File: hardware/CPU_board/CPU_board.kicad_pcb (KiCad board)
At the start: 4 copper layers, 51.2 x 25.8 mm, 111 parts, among them J1 TF TF-018 1.5mm, J2 SOUTH, J3 NORTH, J4 Conn_01x6_Male, J5 Conn_01x03, J6 JTAG, J8 Conn_01x10_Male, U1 EA3036A, U2 W25Q32JVZPIQ, U3 D1s-eLQFP128, U4 PAD30, U5 PAD30, U6 PAD30, U7 PAD30, U8 PAD30, U9 PAD30, X1 24MHz, X2 32.768KHz

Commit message: fixed mixup of pins G5/G4 (3rd diff pair ODD) and DE/PCLK (3rd diff pair EVEN), now with correct polarity for diff pairs
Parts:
- added R32: 10k, Resistor_SMD:R_0402_1005Metric, B.Cu at (101.6, 103.3)
- added R35: 10k, Resistor_SMD:R_0402_1005Metric, B.Cu at (101.6, 102.3)
- added R36: 10k, Resistor_SMD:R_0402_1005Metric, B.Cu at (105.2, 111.0)
- added R40: 10k, Resistor_SMD:R_0402_1005Metric, B.Cu at (106.2, 111.0)
- moved R30 3.79 mm to (107.0, 105.5)
- moved C37 3.05 mm to (105.0, 113.7), turned to -90 degrees
- moved C2 1.88 mm to (106.2, 113.9), turned to 90 degrees
- moved G*** 1.56 mm to (103.8, 102.9)
- moved R21 0.41 mm to (99.7, 105.2)
- moved C4 0.40 mm to (99.7, 106.1)
- moved C7 0.38 mm to (99.7, 104.2)
- moved C5 0.38 mm to (99.7, 103.3)
- moved C35 0.31 mm to (101.9, 109.9)
- moved C32 0.25 mm to (100.0, 109.9)
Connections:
- J2 pad 3: /LCD_V3P -> /LCD_V3N
- J2 pad 5: /LCD_V3N -> /LCD_V3P
- J3 pad 3: /LCD_U3P -> /LCD_U3N
- J3 pad 5: /LCD_U3N -> /LCD_U3P
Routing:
- net GND: track 210.5 -> 189.6 mm, vias 55 -> 54
- net 3V3: track 213.4 -> 226.3 mm
- net /PSEL: track 23.2 -> 13.5 mm
- net /SDA2: track 8.75 -> 12.4 mm
- net VSYS: track 24.0 -> 21.8 mm
- net /SCK: track 24.1 -> 22.4 mm
- net /SDA: track 24.8 -> 23.2 mm
- net /SCK2: track 8.59 -> 10.2 mm
- net /LCD_V3N: track 15.9 -> 14.4 mm
- net /LCD_D9: track 18.7 -> 17.8 mm
- net /X32KIN: track 6.42 -> 5.52 mm
- net /TP-Y2: track 24.7 -> 25.5 mm
- net /LCD_D8: track 19.7 -> 20.5 mm
- net /LCD_U3P: track 13.3 -> 14.1 mm
- net /LCD_V3P: track 14.0 -> 14.6 mm
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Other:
- board text added: "CPU board v0.11"
- board text added: "VERSION:"
- board text removed: "CPU board"
- board text removed: "Memory Card"

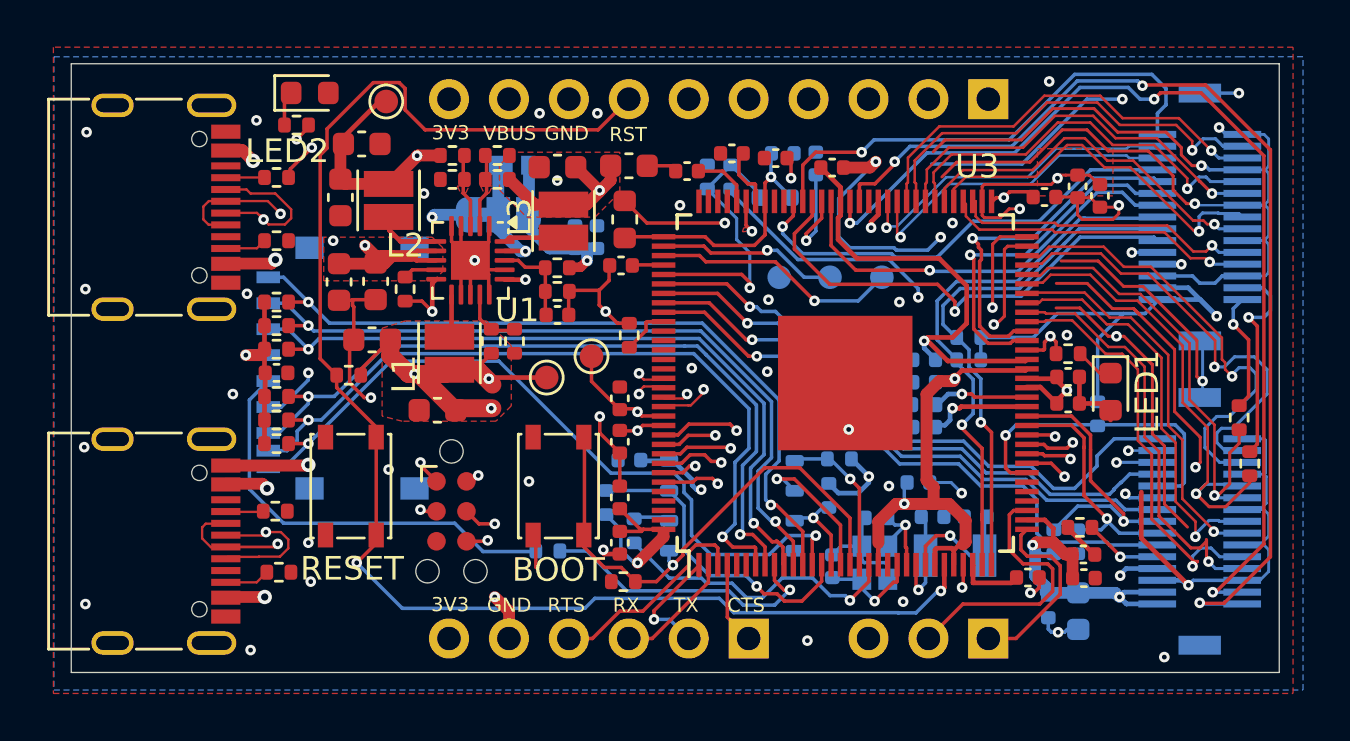
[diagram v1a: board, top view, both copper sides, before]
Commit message: review and update manufacturing constraints (via size, etc.)
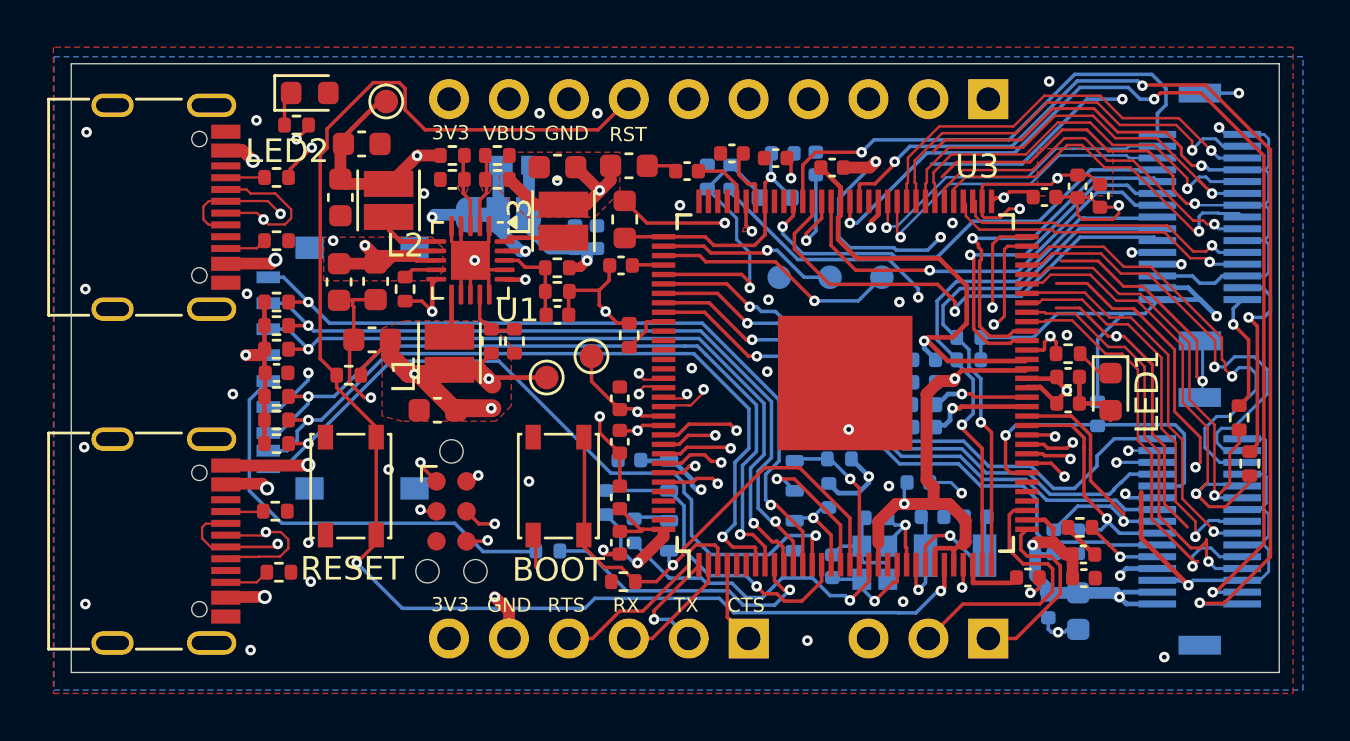
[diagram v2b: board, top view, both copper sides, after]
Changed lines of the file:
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@@
 	(via
 		(at 73.5928 107.702)
-		(size 0.6096)
-		(drill 0.3048)
+		(size 0.6)
+		(drill 0.35)
 		(layers "F.Cu" "B.Cu")
 		(net 14)
@@
 	)
 	(segment
+		(start 80.996048 111.377)
+		(end 83.2078 111.377)
+		(width 0.15)
+		(layer "B.Cu")
+		(net 21)
+	)
+	(segment
+		(start 72.4678 110.177)
+		(end 79.796048 110.177)
+		(width 0.15)
+		(layer "B.Cu")
+		(net 21)
+	)
+	(segment
+		(start 79.796048 110.177)
+		(end 80.996048 111.377)
+		(width 0.15)
+		(layer "B.Cu")
+		(net 21)
+	)
+	(segment
+		(start 71.0928 104.952)
+		(end 71.0928 108.802)
+		(width 0.15)
+		(layer "B.Cu")
+		(net 21)
+	)
+	(segment
+		(start 83.2078 111.377)
+		(end 83.2328 111.352)
+		(width 0.15)
+		(layer "B.Cu")
+		(net 21)
+	)
+	(segment
+		(start 71.0928 108.802)
+		(end 72.4678 110.177)
+		(width 0.15)
+		(layer "B.Cu")
+		(net 21)
+	)
+	(segment
 		(start 71.8928 104.152)
 		(end 71.0928 104.952)
-		(width 0.15)
-		(layer "B.Cu")
-		(net 21)
-	)
-	(segment
-		(start 83.2078 111.377)
-		(end 83.2328 111.352)
-		(width 0.15)
-		(layer "B.Cu")
-		(net 21)
-	)
-	(segment
-		(start 71.0928 108.727)
-		(end 72.5428 110.177)
-		(width 0.15)
-		(layer "B.Cu")
-		(net 21)
-	)
-	(segment
-		(start 72.5428 110.177)
-		(end 79.796048 110.177)
-		(width 0.15)
-		(layer "B.Cu")
-		(net 21)
-	)
-	(segment
-		(start 79.796048 110.177)
-		(end 80.996048 111.377)
-		(width 0.15)
-		(layer "B.Cu")
-		(net 21)
-	)
-	(segment
-		(start 80.996048 111.377)
-		(end 83.2078 111.377)
-		(width 0.15)
-		(layer "B.Cu")
-		(net 21)
-	)
-	(segment
-		(start 71.0928 104.952)
-		(end 71.0928 108.727)
 		(width 0.15)
 		(layer "B.Cu")
@@
 	(via
 		(at 71.8428 108.702)
-		(size 0.6096)
-		(drill 0.3048)
+		(size 0.6)
+		(drill 0.35)
 		(layers "F.Cu" "B.Cu")
 		(net 41)
@@
 	(via
 		(at 71.247828 94.817428)
-		(size 0.6096)
-		(drill 0.3048)
+		(size 0.6)
+		(drill 0.35)
 		(layers "F.Cu" "B.Cu")
 		(net 41)
@@
 	(via
 		(at 72.19733 99.00653)
-		(size 0.6096)
-		(drill 0.3048)
+		(size 0.6)
+		(drill 0.35)
 		(layers "F.Cu" "B.Cu")
 		(net 41)
@@
 	(via
 		(at 71.7428 113.302)
-		(size 0.6096)
-		(drill 0.3048)
+		(size 0.6)
+		(drill 0.35)
 		(layers "F.Cu" "B.Cu")
 		(net 41)

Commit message: add JST connector for I2C
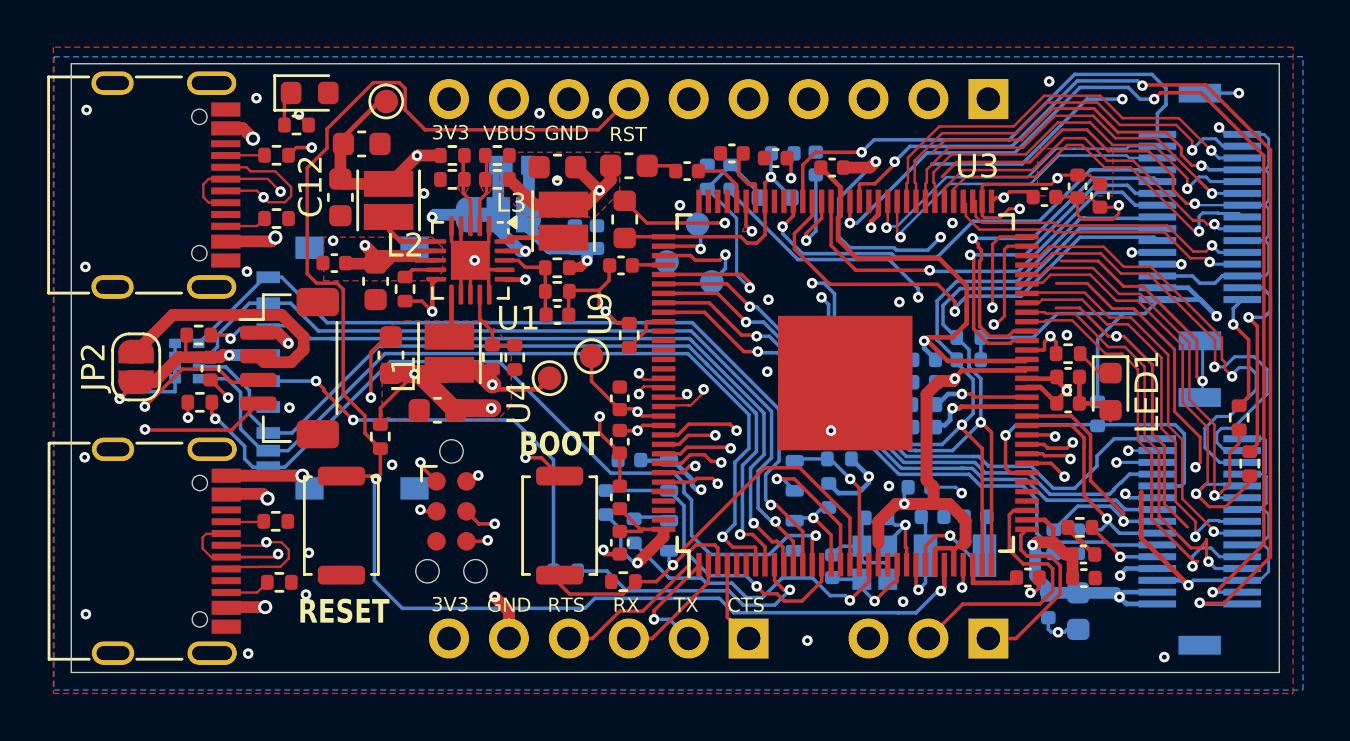
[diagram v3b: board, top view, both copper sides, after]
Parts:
- removed FEL1: FEL, Button_Switch_SMD:SW_SPST_PTS810
- removed R11, R13, R14, R17: 47k, Resistor_SMD:R_0402_1005Metric
- removed RESET1: RESET, Button_Switch_SMD:SW_SPST_PTS810
- added CN1: BM04B-SRSS-TB, Connector_JST:JST_SH_BM04B-SRSS-TB_1x04-1MP_P1.00mm_Vertical, F.Cu at (72.8, 103.6)
- added JP2: SolderJumper_2_Open, Jumper:SolderJumper-2_P1.3mm_Open_RoundedPad1.0x1.5mm, F.Cu at (66.3, 103.6)
- added RN7: 10K, Resistor_SMD:R_Array_Convex_4x0402, B.Cu at (68.4, 103.3)
- added SW1: BOOT, Button_Switch_SMD:SW_Push_SPST_NO_Alps_SKRK, F.Cu at (84.2, 110.3)
- added SW2: RESET, Button_Switch_SMD:SW_Push_SPST_NO_Alps_SKRK, F.Cu at (75.0, 110.3)
- C12: footprint Capacitor_SMD:C_0603_1608Metric -> Capacitor_SMD:C_0402_1005Metric
- moved U6 7.21 mm to (90.7, 100.0)
- moved U7 6.04 mm to (90.1, 97.5)
- moved R1 4.88 mm to (68.9, 102.2)
- moved U5 4.80 mm to (88.8, 99.1)
- moved R15 3.69 mm to (69.0, 105.1)
- moved R19 2.92 mm to (76.6, 106.5), turned to -90 degrees
- moved C31 2.81 mm to (69.4, 103.6), turned to 90 degrees
- moved R16 1.13 mm to (84.5, 112.2)
- moved C14 1.03 mm to (77.1, 103.1), turned to -90 degrees
- moved R29 0.94 mm to (72.2, 94.6)
- moved R27 0.94 mm to (72.2, 97.3)
- moved USB1 0.94 mm to (66.4, 95.8)
- moved C12 0.82 mm to (74.7, 99.2), turned to 0 degrees
- moved R4 0.69 mm to (82.3, 103.2)
- moved R2 0.68 mm to (81.4, 103.1)
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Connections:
- R1 pad 2: /SDC0_D1 -> /SDC0_CMD
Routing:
- net /SCK: track 22.4 -> 79.3 mm, vias 1 -> 3
- net /SDA: track 23.2 -> 79.5 mm, vias 1 -> 3
- net Net-(CN1-Pin_2): track 0.00 -> 10.9 mm
- net /HPOUTL: track 10.4 -> 4.16 mm
- net /HPOUTR: track 7.65 -> 2.68 mm
- net 3V3: track 226.3 -> 230.8 mm, vias 19 -> 21
- net GND: track 189.6 -> 185.4 mm
- net /SDC0_D1: track 32.2 -> 36.2 mm, vias 2 -> 1
- net /SDC0_D0: track 32.0 -> 35.6 mm, vias 2 -> 1
- net /SDC2_D2: track 22.3 -> 18.7 mm
- net /SDC0_CD: track 31.9 -> 35.4 mm
- net /SDC0_D3: track 31.6 -> 34.8 mm, vias 2 -> 1
- net /SDC0_D2: track 32.6 -> 35.7 mm, vias 2 -> 1
- net /RST: track 62.9 -> 64.9 mm
- net /SDC0_CMD: track 31.3 -> 33.1 mm
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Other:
- board text added: "CPU v0.11"
- board text removed: "CPU board v0.11"

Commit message: move and add resistor arrayas as pullups for SD, fix R0/R1 mixup
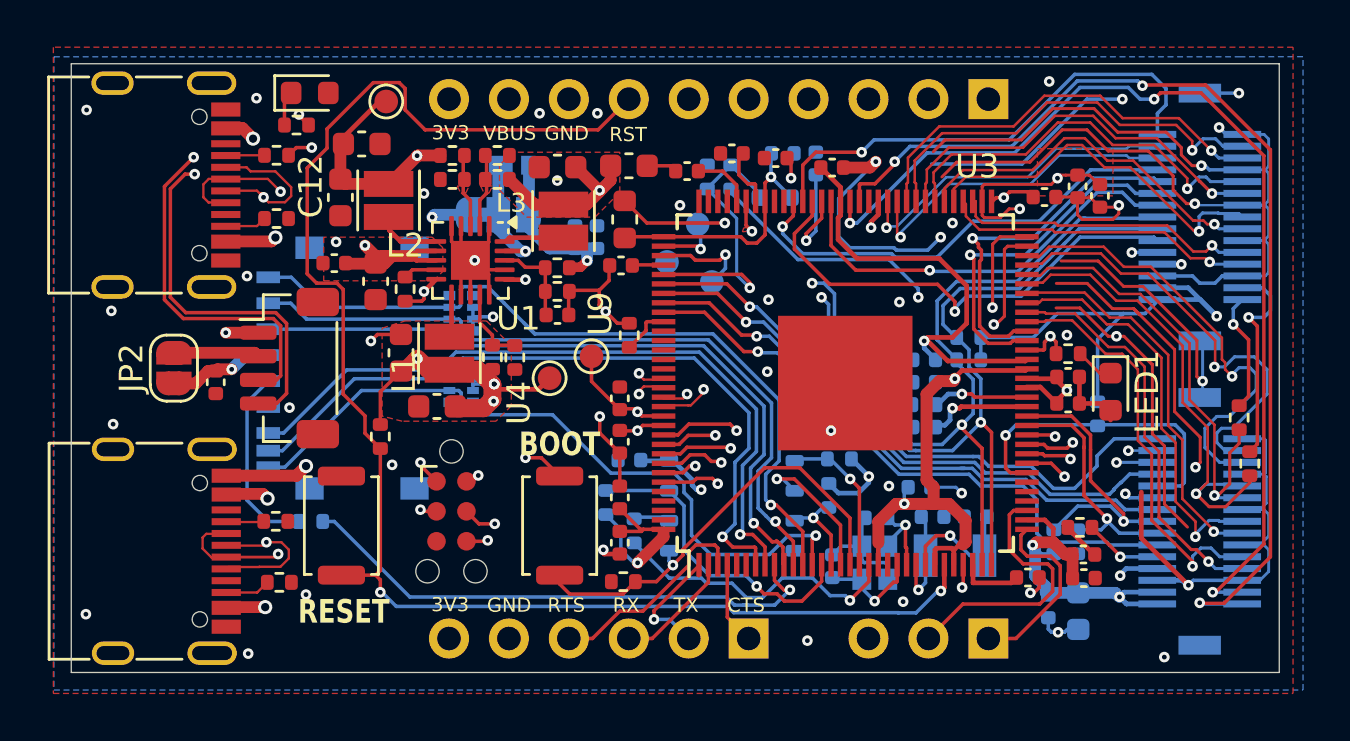
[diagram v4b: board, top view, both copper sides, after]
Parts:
- removed R1, R15: 47k, Resistor_SMD:R_0402_1005Metric
- added RN1: 47K, Resistor_SMD:R_Array_Convex_4x0402, B.Cu at (80.1, 104.3)
- RN7: value 10K -> 47K
- moved RN7 11.8 mm to (80.1, 101.3)
- moved R16 11.0 mm to (73.7, 110.1)
- moved JP2 1.60 mm to (67.9, 103.6)
- moved C31 0.62 mm to (69.7, 104.2)
- moved C14 0.44 mm to (77.5, 103.0)
- moved C13 0.16 mm to (79.0, 105.2)
- turned SW2 to 90 degrees
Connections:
- RN7 pad 1: 3V3 -> /SDC0_CMD
- RN7 pad 2: 3V3 -> /SDC0_D3
- RN7 pad 3: 3V3 -> /SDC0_D2
- RN7 pad 4: 3V3 -> unconnected-(RN7-R4.1-Pad4)
- RN7 pad 5: /SDC0_D2 -> unconnected-(RN7-R4.2-Pad5)
- RN7 pad 6: /SDC0_D3 -> 3V3
- RN7 pad 7: /SDC0_D0 -> 3V3
- RN7 pad 8: /SDC0_D1 -> 3V3
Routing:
- net Net-(U3-PF2): track 11.2 -> 23.2 mm
- net /SDC0_CLK: track 18.2 -> 7.99 mm, vias 2 -> 0
- net 3V3: track 230.8 -> 223.4 mm
- net Net-(CN1-Pin_2): track 10.9 -> 3.64 mm
- net /SDC0_CD: track 35.4 -> 30.6 mm, vias 2 -> 1
- net /SDC0_D1: track 36.2 -> 31.5 mm
- net /SDC0_D0: track 35.6 -> 30.9 mm
- net GND: track 185.4 -> 180.9 mm, vias 54 -> 51
- net /SDC0_D3: track 34.8 -> 31.2 mm
- net /SDC0_CMD: track 33.1 -> 30.3 mm, vias 2 -> 1
- net /SDC0_D2: track 35.7 -> 33.8 mm
- net VBUS: track 108.4 -> 106.8 mm
- net /SDA: track 79.5 -> 78.4 mm
- net /SCK: track 79.3 -> 78.2 mm
- net /LCD_V0N: track 18.0 -> 17.1 mm
